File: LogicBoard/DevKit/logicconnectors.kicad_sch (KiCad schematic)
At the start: 32 parts, among them J1 ServoConn, J1 USBC Socket, J10 PhaseConn1, J18 PhaseConn1, J19 PhaseConn1, J2 AuxConn, J4 ADCConn, J5 HallConn, J6 UartSpi, J7 JTAG, J8 CANConn, U10 HM-10, U2 USBLC6-2P6, U6 TJA1051T-3

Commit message: v2
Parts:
- removed J4: ADCConn, Connector_JST:JST_XH_S6B-XH-A_1x06_P2.50mm_Horizontal, symbol Connector:Conn_01x06_Pin
- removed J6: UartSpi, Connector_JST:JST_XH_S5B-XH-A_1x05_P2.50mm_Horizontal, symbol Connector:Conn_01x05_Pin
- removed U10: HM-10, GigaVescLibs:HM10, symbol GigaVescSymbols:HM-10
- added J11: SPI1Conn, Connector_JST:JST_PH_S6B-PH-K_1x06_P2.00mm_Horizontal, symbol Connector:Conn_01x06_Pin
- added J20: UART2Conn, Connector_JST:JST_PH_S4B-PH-K_1x04_P2.00mm_Horizontal, symbol Connector:Conn_01x04_Pin
- added J6: UARTConn, Connector_JST:JST_PH_S4B-PH-K_1x04_P2.00mm_Horizontal, symbol Connector:Conn_01x04_Pin
- C24, C26, C5: footprint Capacitor_SMD:C_0805_2012Metric -> Capacitor_SMD:C_0603_1608Metric; MPN (none) -> C14663
- C25: footprint Capacitor_SMD:C_0805_2012Metric -> Capacitor_SMD:C_0603_1608Metric; MPN (none) -> C15849
- C27: footprint Capacitor_SMD:C_0805_2012Metric -> Capacitor_SMD:C_0603_1608Metric; MPN C49217 -> C23630
- J1, J8: footprint Connector_JST:JST_XH_S4B-XH-A_1x04_P2.50mm_Horizontal -> Connector_JST:JST_PH_S4B-PH-K_1x04_P2.00mm_Horizontal; JLCPosOffset -3.75,0 -> 3,0; JLCRotOffset -180 -> 0; MPN C157925 -> C157926
- J2: footprint Connector_JST:JST_XH_S8B-XH-A_1x08_P2.50mm_Horizontal -> Connector_JST:JST_PH_S8B-PH-K_1x08_P2.00mm_Horizontal; JLCPosOffset -8.75,0 -> -7,0; MPN C157914 -> C157915
- J5: footprint Connector_JST:JST_XH_S6B-XH-A_1x06_P2.50mm_Horizontal -> Connector_JST:JST_PH_S6B-PH-K_1x06_P2.00mm_Horizontal; JLCPosOffset -6.25,0 -> 5,0; JLCRotOffset -180 -> 0; MPN C157919 -> C157920
- R1: footprint Resistor_SMD:R_0805_2012Metric -> Resistor_SMD:R_0603_1608Metric; MPN (none) -> C25804
- R1: footprint Resistor_SMD:R_0805_2012Metric -> Resistor_SMD:R_0603_1608Metric; MPN C17557 -> C22962
- R1: footprint Resistor_SMD:R_0805_2012Metric -> Resistor_SMD:R_0603_1608Metric; MPN (none) -> C4190
- R1: footprint Resistor_SMD:R_0805_2012Metric -> Resistor_SMD:R_0603_1608Metric; MPN (none) -> C22775
- R1: footprint Resistor_SMD:R_0805_2012Metric -> Resistor_SMD:R_0603_1608Metric; MPN C17408 -> C22775
- R21: footprint Resistor_SMD:R_0805_2012Metric -> Resistor_SMD:R_0603_1608Metric; MPN C17437 -> C22787
- R3: footprint Resistor_SMD:R_0805_2012Metric -> Resistor_SMD:R_0603_1608Metric; MPN (none) -> C23345
- R4: footprint Resistor_SMD:R_0805_2012Metric -> Resistor_SMD:R_0603_1608Metric; MPN C17561 -> C23345
- R5: footprint Resistor_SMD:R_0805_2012Metric -> Resistor_SMD:R_0603_1608Metric; MPN C27834 -> C23186
- R6: footprint Resistor_SMD:R_0805_2012Metric -> Resistor_SMD:R_0603_1608Metric; MPN (none) -> C23186
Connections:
- net +3.3V: now also J11.1 (Pin_1), J20.1 (Pin_1), J6.1 (Pin_1)
- net GND: now also J11.6 (Pin_6), J20.4 (Pin_4), J6.4 (Pin_4)
- net CANRx renamed CAN_RX
- net CANTx renamed CAN_TX
- net MISO_ADC_EXT2 renamed ADC_EXT2
- net SCK_ADC_EXT renamed ADC_EXT
- net SENS_FILTER_ENABLE renamed PHASE_FILTER_ENABLE
- new net EXT2_RX: J20.2 (Pin_2)
- new net EXT2_TX: J20.3 (Pin_3)
- new net EXT_RX: J6.3 (Pin_3)
- new net EXT_TX: J6.2 (Pin_2)
- new net SPI1_MISO: J11.4 (Pin_4)
- new net SPI1_MOSI: J11.5 (Pin_5)
- new net SPI1_NSS: J11.2 (Pin_2)
- new net SPI1_SCK: J11.3 (Pin_3)
- no-connect marks 18 -> 2
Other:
- note added: "Mutually exclusive with SPI1"
- note added: "SPI1 PA15 PA5 PA6 PA7"
- moved on the sheet: C5, J1, J2, J5, R1

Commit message: v2
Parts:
- removed C25: 1u, Capacitor_SMD:C_0603_1608Metric, symbol Device:C
- removed R1: 2.2k, Resistor_SMD:R_0603_1608Metric, symbol Device:R
- removed R1 (x3): 100, Resistor_SMD:R_0603_1608Metric, symbol Device:R
- removed R1: 10k, Resistor_SMD:R_0603_1608Metric, symbol Device:R
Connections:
- net HALL1_IN: now also J5.4 (Pin_4)
- net HALL2_IN: now also J5.3 (Pin_3)
- net HALL3_IN: now also J5.2 (Pin_2)

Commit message: initialv2
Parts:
- removed J20: UART2Conn, Connector_JST:JST_PH_S4B-PH-K_1x04_P2.00mm_Horizontal, symbol Connector:Conn_01x04_Pin
- added J12: UART2Conn, Connector_JST:JST_PH_B4B-PH-K_1x04_P2.00mm_Vertical, symbol Connector:Conn_01x04_Pin
- added J20: SPI1Conn, Connector_JST:JST_PH_S6B-PH-K_1x06_P2.00mm_Horizontal, symbol Connector:Conn_01x06_Pin
- added J22: UART3Conn, Connector_JST:JST_PH_B4B-PH-K_1x04_P2.00mm_Vertical, symbol Connector:Conn_01x04_Pin
- J7: footprint Connector_PinHeader_2.54mm:PinHeader_2x02_P2.54mm_Vertical_SMD -> Connector_PinHeader_2.54mm:PinHeader_2x02_P2.54mm_Vertical; MPN C919361 -> C2685136
- U6: value TJA1051T-3 -> TJA1050T/CM,118; MPN C5342108 -> C6952
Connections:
- net +3.3V: now also J12.1 (Pin_1), J20.1 (Pin_1), J22.1 (Pin_1)
- net ADC_EXT2: now also R1.1; no longer R1.2
- net GND: now also R1.2, J12.4 (Pin_4), J20.6 (Pin_6), J22.4 (Pin_4); no longer R1.1
- net EXT_RX renamed I2C2_SDA/USART3_RX
- net EXT_TX renamed I2C2_SCL/USART3_TX
- new net SPI3_MISO: J20.4 (Pin_4)
- new net SPI3_MOSI: J20.5 (Pin_5)
- new net SPI3_NSS: J20.2 (Pin_2)
- new net SPI3_SCK: J20.3 (Pin_3)
- new net UART3_RX: J22.3 (Pin_3)
- new net UART3_TX: J22.2 (Pin_2)
- new net USART2_RX: J12.3 (Pin_3)
- new net USART2_TX: J12.2 (Pin_2)
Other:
- note added: "Angled connectors"
- note added: "Newer Alternative TJA1051T/3 C5342108"
- note added: "Straight connectors"
- moved on the sheet: J5, R1

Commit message: v2
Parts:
- removed U2: USBLC6-2P6, Package_TO_SOT_SMD:SOT-666, symbol Power_Protection:USBLC6-2P6
- added U7: USBLC6-2SC6, Package_TO_SOT_SMD:SOT-23-6, symbol Power_Protection:USBLC6-2P6
- C24, C26, C27, C5: footprint Capacitor_SMD:C_0603_1608Metric -> GigaVescLibs:C_0603_1608Metric_L
- J12, J22: JLCPosOffset 3,0 -> -3,0; JLCRotOffset 0 -> 180
- J7: JLCPosOffset (none) -> 1.27,1.27
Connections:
- net GND: now also U7.2 (GND)
- net at J1.A4 (VBUS), J1.A9 (VBUS), J1.B4 (VBUS)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: now also U7.5 (VBUS)
- net at J1.A6 (D+), J1.B6 (D+): now also U7.6 (I/O1)
- net at J1.A7 (D-), J1.B7 (D-): now also U7.4 (I/O2)
- net at R3.1: now also U7.3 (I/O2)
- net at R4.1: now also U7.1 (I/O1)
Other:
- note added: "Can be omitted inserting pins works just fine"
- note added: "Can be ommited on budget connect line 1-6 and 3-4"
- note added: "Straight connectors Can be omitted"
- note added: "TJA1050 is slower (1M baud, still maxes out) but it is a basic component"
- note removed: "Straight connectors"
- note removed: "TODO: Verify this if CANH/L Needs any pullups or additional stuff"
- moved on the sheet: J1, J10, J18, J19, J2, J7, R3, R4, R5, R6

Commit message: wholeDevice
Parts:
- J10, J18, J19: footprint Connector_PinHeader_2.54mm:PinHeader_2x03_P2.54mm_Vertical -> Connector_PinHeader_2.54mm:PinHeader_2x03_P2.54mm_Vertical_SMD; MPN C65114 -> C780054
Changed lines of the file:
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@@
       (effects (font (size 1.27 1.27)))
     )
-    (property "Footprint" "Connector_PinHeader_2.54mm:PinHeader_2x03_P2.54mm_Vertical" (at 240.03 64.77 0)
+    (property "Footprint" "Connector_PinHeader_2.54mm:PinHeader_2x03_P2.54mm_Vertical_SMD" (at 240.03 64.77 0)
       (effects (font (size 1.27 1.27)) hide)
     )
@@
       (effects (font (size 1.27 1.27)) hide)
     )
-    (property "MPN" "C65114" (at 240.03 64.77 0)
+    (property "MPN" "C780054" (at 240.03 64.77 0)
       (effects (font (size 1.27 1.27)) hide)
     )
@@
       (effects (font (size 1.27 1.27)))
     )
-    (property "Footprint" "Connector_PinHeader_2.54mm:PinHeader_2x03_P2.54mm_Vertical" (at 240.03 34.29 0)
+    (property "Footprint" "Connector_PinHeader_2.54mm:PinHeader_2x03_P2.54mm_Vertical_SMD" (at 240.03 34.29 0)
       (effects (font (size 1.27 1.27)) hide)
     )
@@
       (effects (font (size 1.27 1.27)) hide)
     )
-    (property "MPN" "C65114" (at 240.03 34.29 0)
+    (property "MPN" "C780054" (at 240.03 34.29 0)
       (effects (font (size 1.27 1.27)) hide)
     )
@@
       (effects (font (size 1.27 1.27)))
     )
-    (property "Footprint" "Connector_PinHeader_2.54mm:PinHeader_2x03_P2.54mm_Vertical" (at 240.03 49.53 0)
+    (property "Footprint" "Connector_PinHeader_2.54mm:PinHeader_2x03_P2.54mm_Vertical_SMD" (at 240.03 49.53 0)
       (effects (font (size 1.27 1.27)) hide)
     )
@@
       (effects (font (size 1.27 1.27)) hide)
     )
-    (property "MPN" "C65114" (at 240.03 49.53 0)
-      (effects (font (size 1.27 1.27)) hide)
-    )
+    (property "MPN" "C780054" (at 240.03 49.53 0)
+      (effects (font (size 1.27 1.27)) hide)
+    )

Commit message: minor
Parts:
- J7: MPN C2685136 -> (none); MPNx (none) -> C2685136
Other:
- note added: "Can be omitted, replaced MPN so its not exported with bom inserting pins works just fine"
- note removed: "Can be omitted inserting pins works just fine"
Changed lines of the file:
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@@
     (fill (type none))
   )
-  (text "Can be omitted\ninserting pins works just fine" (at 123.19 99.06 0)
+  (text "Can be omitted, replaced MPN so its not exported with bom\ninserting pins works just fine"
+    (at 107.95 100.33 0)
     (effects (font (size 1.27 1.27)) (justify left bottom))
   )
@@
       (effects (font (size 1.27 1.27)) hide)
     )
-    (property "MPN" "C2685136" (at 134.62 88.9 0)
-      (effects (font (size 1.27 1.27)) hide)
-    )
+    (property "MPNx" "C2685136" (at 134.62 88.9 0)
+      (effects (font (size 1.27 1.27)) hide)
+    )

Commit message: v2.3
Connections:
- net CURR1: no longer J10.6 (Pin_6)
- net CURR2: no longer J18.6 (Pin_6)
- net CURR3: no longer J19.6 (Pin_6)
- removed net PHASE_FILTER_ENABLE: J10.3 (Pin_3), J18.3 (Pin_3), J19.3 (Pin_3)
- new net SH+1_IN: J10.6 (Pin_6)
- new net SH+2_IN: J18.6 (Pin_6)
- new net SH+3_IN: J19.6 (Pin_6)
- new net SH-1_IN: J10.3 (Pin_3)
- new net SH-2_IN: J18.3 (Pin_3)
- new net SH-3_IN: J19.3 (Pin_3)
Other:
- added sheet ShuntAmp1 (ShuntAmp.kicad_sch)
- added sheet ShuntAmp2 (ShuntAmp.kicad_sch)
- added sheet ShuntAmp3 (ShuntAmp.kicad_sch)
- moved on the sheet: J1, J10, J18, J19, J2, J7, R3, R4, R5, R6, U7

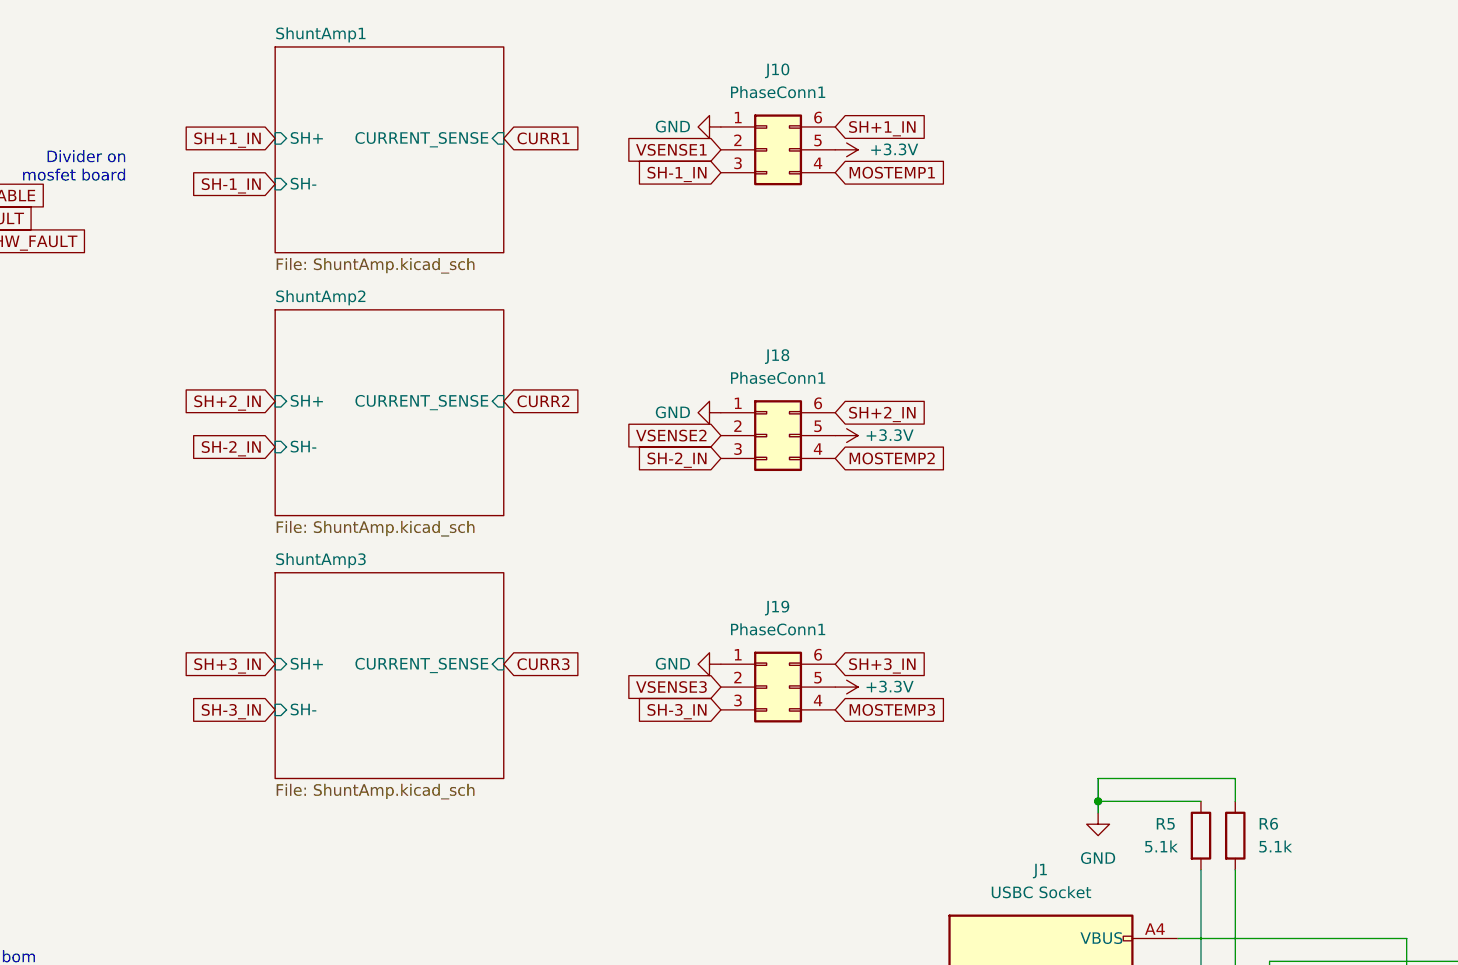
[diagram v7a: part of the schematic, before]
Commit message: v2.4 - INA4181A1IPWR
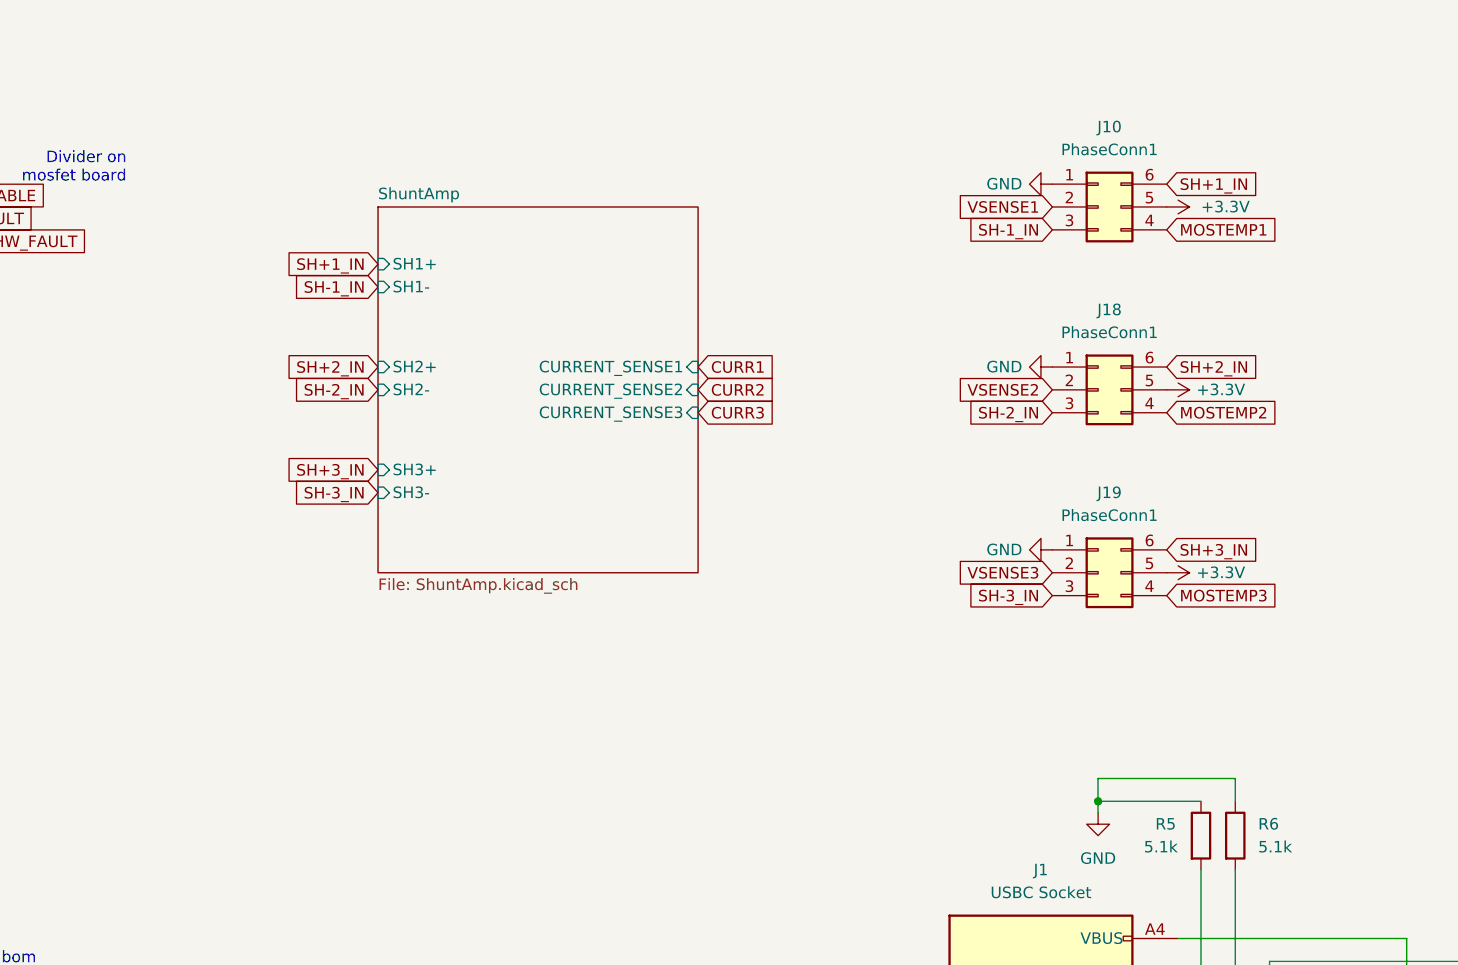
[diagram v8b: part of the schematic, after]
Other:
- sheet ShuntAmp1 renamed ShuntAmp
- removed sheet ShuntAmp2
- removed sheet ShuntAmp3
- sheet ShuntAmp ports: added CURRENT_SENSE1, CURRENT_SENSE2, CURRENT_SENSE3, SH1+, SH1-, SH2+, SH2-, SH3+, SH3-; removed CURRENT_SENSE, SH+, SH-
- moved on the sheet: J10, J18, J19
